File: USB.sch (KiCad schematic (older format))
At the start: 6 parts, among them IC1 TPD2E1B06, J5 USB_OTG

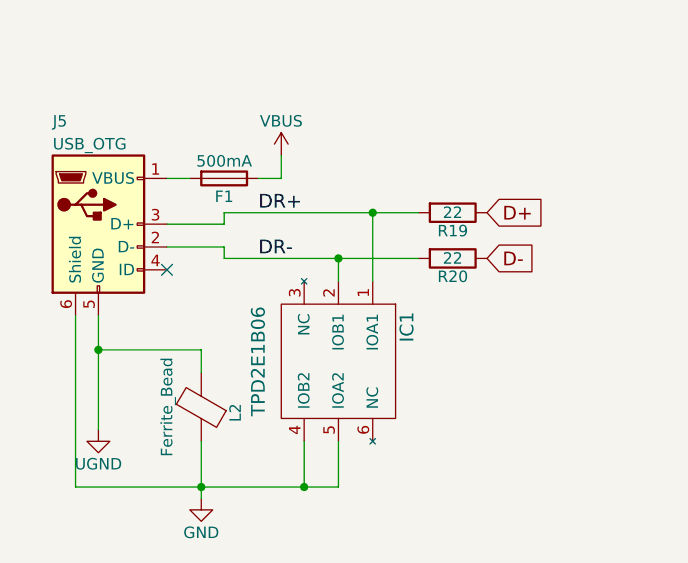
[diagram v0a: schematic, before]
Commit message: Board should be ok. Bargraph leds yet to do.
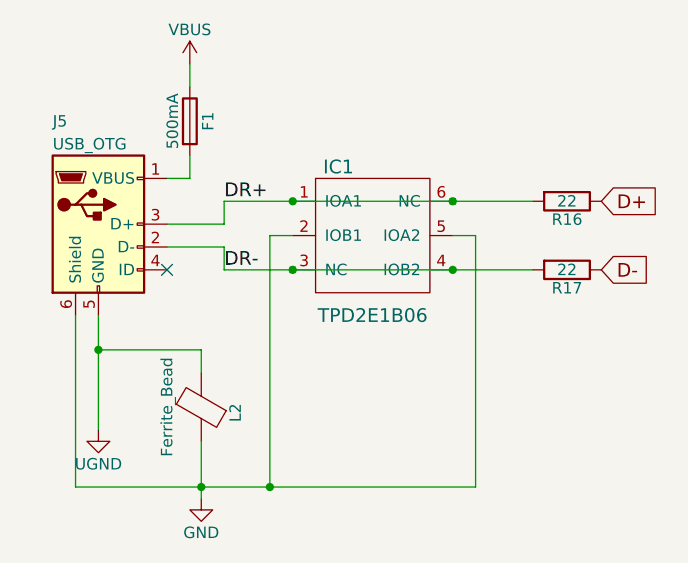
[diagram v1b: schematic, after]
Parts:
- renumbered R19 to R16, R20 to R17
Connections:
- net DR+: now also IC1.6 (NC)
- net DR-: now also IC1.3 (NC), IC1.4 (IOB2); no longer IC1.2 (IOB1)
- net GND: now also IC1.2 (IOB1); no longer IC1.4 (IOB2)
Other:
- moved on the sheet: F1, IC1, R16, R17
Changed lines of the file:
@@
 	1700 4150 1700 4650
 $Comp
-L R R19
+L R R16
 U 1 1 59A9734A
-P 3250 3700
-F 0 "R19" V 3330 3700 50  0000 C CNN
-F 1 "22" V 3250 3700 50  0000 C CNN
-F 2 "Resistors_SMD:R_0603" V 3180 3700 50  0001 C CNN
-F 3 "" H 3250 3700 50  0001 C CNN
-	1    3250 3700
+P 3750 3650
+F 0 "R16" V 3830 3650 50  0000 C CNN
+F 1 "22" V 3750 3650 50  0000 C CNN
+F 2 "Resistors_SMD:R_0603" V 3680 3650 50  0001 C CNN
+F 3 "" H 3750 3650 50  0001 C CNN
+	1    3750 3650
 	0    1    1    0
 $EndComp
 $Comp
-L R R20
+L R R17
 U 1 1 59A973A2
-P 3250 3900
-F 0 "R20" V 3330 3900 50  0000 C CNN
-F 1 "22" V 3250 3900 50  0000 C CNN
-F 2 "Resistors_SMD:R_0603" V 3180 3900 50  0001 C CNN
-F 3 "" H 3250 3900 50  0001 C CNN
-	1    3250 3900
+P 3750 3950
+F 0 "R17" V 3830 3950 50  0000 C CNN
+F 1 "22" V 3750 3950 50  0000 C CNN
+F 2 "Resistors_SMD:R_0603" V 3680 3950 50  0001 C CNN
+F 3 "" H 3750 3950 50  0001 C CNN
+	1    3750 3950
 	0    1    1    0
 $EndComp
@@
 	2000 3850 2250 3850
 Wire Wire Line
-	2250 3850 2250 3900
-Wire Wire Line
-	2250 3900 3100 3900
-Wire Wire Line
 	2000 3750 2250 3750
-Wire Wire Line
-	2250 3750 2250 3700
-Wire Wire Line
-	2250 3700 3100 3700
-Text GLabel 3400 3700 2    60   Input ~ 0
+Text GLabel 3900 3650 2    60   Input ~ 0
 D+
-Text GLabel 3400 3900 2    60   Input ~ 0
+Text GLabel 3900 3950 2    60   Input ~ 0
 D-
 NoConn ~ 2000 3950
-Wire Wire Line
-	2900 4000 2900 3700
-Connection ~ 2900 3700
 $Comp
 L GND #PWR036
@@
 $EndComp
 Wire Wire Line
-	2750 4900 2750 4700
-Wire Wire Line
-	1600 4900 2750 4900
+	1600 4900 3350 4900
 Wire Wire Line
 	2150 4700 2150 4950
@@
 L VBUS #PWR037
 U 1 1 59A98508
-P 2500 3450
-F 0 "#PWR037" H 2500 3300 50  0001 C CNN
-F 1 "VBUS" H 2500 3600 50  0000 C CNN
-F 2 "" H 2500 3450 50  0001 C CNN
-F 3 "" H 2500 3450 50  0001 C CNN
-	1    2500 3450
+P 2100 3050
+F 0 "#PWR037" H 2100 2900 50  0001 C CNN
+F 1 "VBUS" H 2100 3200 50  0000 C CNN
+F 2 "" H 2100 3050 50  0001 C CNN
+F 3 "" H 2100 3050 50  0001 C CNN
+	1    2100 3050
 	1    0    0    -1
 $EndComp
@@
 L Fuse F1
 U 1 1 59B07000
-P 2250 3550
-F 0 "F1" V 2330 3550 50  0000 C CNN
-F 1 "500mA" V 2175 3550 50  0000 C CNN
-F 2 "Fuse_Holders_and_Fuses:Fuse_SMD1206_Reflow" V 2180 3550 50  0001 C CNN
-F 3 "" H 2250 3550 50  0001 C CNN
-	1    2250 3550
-	0    1    1    0
+P 2100 3300
+F 0 "F1" V 2180 3300 50  0000 C CNN
+F 1 "500mA" V 2025 3300 50  0000 C CNN
+F 2 "Fuse_Holders_and_Fuses:Fuse_SMD1206_Reflow" V 2030 3300 50  0001 C CNN
+F 3 "" H 2100 3300 50  0001 C CNN
+	1    2100 3300
+	1    0    0    -1
 $EndComp
 Wire Wire Line
-	2500 3450 2500 3550
-Wire Wire Line
-	2500 3550 2400 3550
+	2100 3050 2100 3150
 Wire Wire Line
 	2000 3550 2100 3550
@@
 	2150 4300 1700 4300
 Connection ~ 1700 4300
+Text Label 2250 3650 0    60   ~ 0
+DR+
+Text Label 2250 3950 0    60   ~ 0
+DR-
+Wire Wire Line
+	2100 3550 2100 3450
 $Comp
 L TPD2E1B06 IC1
 U 1 1 59C9805E
-P 2750 4350
-F 0 "IC1" H 2600 4650 60  0000 C CNN
-F 1 "TPD2E1B06" H 2750 4000 60  0000 C CNN
-F 2 "IC:SOT-5X3" H 2750 4350 60  0001 C CNN
-F 3 "" H 2750 4350 60  0001 C CNN
-	1    2750 4350
-	0    1    1    0
+P 2900 3800
+F 0 "IC1" H 2750 4100 60  0000 C CNN
+F 1 "TPD2E1B06" H 2900 3450 60  0000 C CNN
+F 2 "IC:SOT-5X3" H 2900 3800 60  0001 C CNN
+F 3 "" H 2900 3800 60  0001 C CNN
+	1    2900 3800
+	1    0    0    -1
 $EndComp
 Wire Wire Line
-	2750 4000 2750 3900
-Connection ~ 2750 3900
+	2250 3850 2250 3950
 Wire Wire Line
-	2600 4700 2600 4900
-Connection ~ 2600 4900
-Text Label 2400 3700 0    60   ~ 0
-DR+
-Text Label 2400 3900 0    60   ~ 0
-DR-
+	2250 3950 3600 3950
+Wire Wire Line
+	2250 3750 2250 3650
+Wire Wire Line
+	2250 3650 3600 3650
+Connection ~ 3250 3650
+Connection ~ 2550 3650
+Wire Wire Line
+	3350 4900 3350 3800
+Wire Wire Line
+	3350 3800 3250 3800
+Wire Wire Line
+	2550 3800 2450 3800
+Wire Wire Line
+	2450 3800 2450 4900
+Connection ~ 2450 4900
+Connection ~ 3250 3950
+Connection ~ 2550 3950
 $EndSCHEMATC

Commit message: Board modified after ckecking. Ready for fab, just need to create gerber, position and components files.
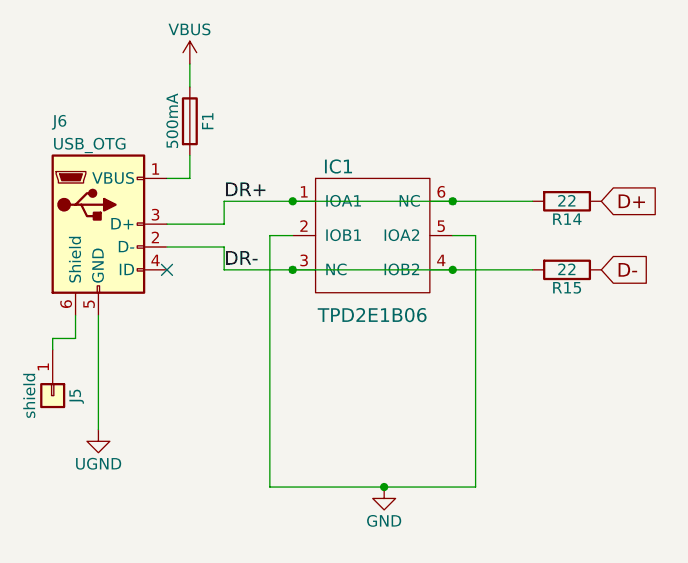
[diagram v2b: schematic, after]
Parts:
- removed L2: Ferrite_Bead, Inductors_SMD:L_0603, symbol Ferrite_Bead
- added J5: shield, Pin_Headers:Pin_Header_Straight_1x01_Pitch2.54mm, symbol Conn_01x01
- renumbered J5 to J6, R16 to R14, R17 to R15
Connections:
- net GND: no longer J6.6 (Shield)
- new net: J5.1 (Pin_1), J6.6 (Shield)
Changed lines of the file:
@@
 EESchema Schematic File Version 2
+LIBS:ContactConsequencesMono-rescue
 LIBS:switches-perso
 LIBS:Logos
@@
 $EndDescr
 $Comp
-L USB_OTG J5
+L USB_OTG J6
 U 1 1 59A96D83
 P 1700 3750
-F 0 "J5" H 1500 4200 50  0000 L CNN
+F 0 "J6" H 1500 4200 50  0000 L CNN
 F 1 "USB_OTG" H 1500 4100 50  0000 L CNN
 F 2 "Connectors:USB_Micro-B" H 1850 3700 50  0001 C CNN
@@
 $EndComp
 $Comp
-L UGND #PWR035
+L UGND #PWR037
 U 1 1 59A9730E
 P 1700 4650
-F 0 "#PWR035" H 1700 4400 50  0001 C CNN
+F 0 "#PWR037" H 1700 4400 50  0001 C CNN
 F 1 "UGND" H 1700 4500 50  0000 C CNN
 F 2 "" H 1700 4650 50  0001 C CNN
@@
 	1    0    0    -1
 $EndComp
-Wire Wire Line
-	1700 4150 1700 4650
-$Comp
-L R R16
+$Comp
+L R R14
 U 1 1 59A9734A
 P 3750 3650
-F 0 "R16" V 3830 3650 50  0000 C CNN
+F 0 "R14" V 3830 3650 50  0000 C CNN
 F 1 "22" V 3750 3650 50  0000 C CNN
 F 2 "Resistors_SMD:R_0603" V 3680 3650 50  0001 C CNN
@@
 $EndComp
 $Comp
-L R R17
+L R R15
 U 1 1 59A973A2
 P 3750 3950
-F 0 "R17" V 3830 3950 50  0000 C CNN
+F 0 "R15" V 3830 3950 50  0000 C CNN
 F 1 "22" V 3750 3950 50  0000 C CNN
 F 2 "Resistors_SMD:R_0603" V 3680 3950 50  0001 C CNN
@@
 	0    1    1    0
 $EndComp
-Wire Wire Line
-	2000 3850 2250 3850
-Wire Wire Line
-	2000 3750 2250 3750
 Text GLabel 3900 3650 2    60   Input ~ 0
 D+
@@
 NoConn ~ 2000 3950
 $Comp
-L GND #PWR036
+L GND #PWR038
 U 1 1 59A98308
-P 2150 4950
-F 0 "#PWR036" H 2150 4700 50  0001 C CNN
-F 1 "GND" H 2150 4800 50  0000 C CNN
-F 2 "" H 2150 4950 50  0001 C CNN
-F 3 "" H 2150 4950 50  0001 C CNN
-	1    2150 4950
-	1    0    0    -1
-$EndComp
-Wire Wire Line
-	1600 4900 3350 4900
-Wire Wire Line
-	2150 4700 2150 4950
-Wire Wire Line
-	1600 4900 1600 4150
-Connection ~ 2150 4900
-$Comp
-L VBUS #PWR037
+P 2950 4900
+F 0 "#PWR038" H 2950 4650 50  0001 C CNN
+F 1 "GND" H 2950 4750 50  0000 C CNN
+F 2 "" H 2950 4900 50  0001 C CNN
+F 3 "" H 2950 4900 50  0001 C CNN
+	1    2950 4900
+	1    0    0    -1
+$EndComp
+$Comp
+L VBUS #PWR039
 U 1 1 59A98508
 P 2100 3050
-F 0 "#PWR037" H 2100 2900 50  0001 C CNN
+F 0 "#PWR039" H 2100 2900 50  0001 C CNN
 F 1 "VBUS" H 2100 3200 50  0000 C CNN
 F 2 "" H 2100 3050 50  0001 C CNN
@@
 	1    0    0    -1
 $EndComp
-Wire Wire Line
-	2100 3050 2100 3150
-Wire Wire Line
-	2000 3550 2100 3550
-$Comp
-L Ferrite_Bead L2
-U 1 1 59B1BF09
-P 2150 4550
-F 0 "L2" V 2000 4575 50  0000 C CNN
-F 1 "Ferrite_Bead" V 2300 4550 50  0000 C CNN
-F 2 "Inductors_SMD:L_0603" V 2080 4550 50  0001 C CNN
-F 3 "" H 2150 4550 50  0001 C CNN
-	1    2150 4550
-	-1   0    0    1
-$EndComp
-Wire Wire Line
-	2150 4400 2150 4300
-Wire Wire Line
-	2150 4300 1700 4300
-Connection ~ 1700 4300
 Text Label 2250 3650 0    60   ~ 0
 DR+
 Text Label 2250 3950 0    60   ~ 0
 DR-
-Wire Wire Line
-	2100 3550 2100 3450
 $Comp
 L TPD2E1B06 IC1
@@
 $EndComp
 Wire Wire Line
+	1700 4150 1700 4650
+Wire Wire Line
+	2000 3850 2250 3850
+Wire Wire Line
+	2000 3750 2250 3750
+Wire Wire Line
+	2100 3050 2100 3150
+Wire Wire Line
+	2000 3550 2100 3550
+Wire Wire Line
+	2100 3550 2100 3450
+Wire Wire Line
 	2250 3850 2250 3950
 Wire Wire Line
@@
 Wire Wire Line
 	2550 3800 2450 3800
-Wire Wire Line
-	2450 3800 2450 4900
-Connection ~ 2450 4900
 Connection ~ 3250 3950
 Connection ~ 2550 3950
+Wire Wire Line
+	2450 3800 2450 4900
+Wire Wire Line
+	2450 4900 3350 4900
+Connection ~ 2950 4900
+$Comp
+L Conn_01x01 J5
+U 1 1 59F09009
+P 1500 4500
+F 0 "J5" H 1500 4600 50  0000 C CNN
+F 1 "shield" H 1500 4400 50  0000 C CNN
+F 2 "Pin_Headers:Pin_Header_Straight_1x01_Pitch2.54mm" H 1500 4500 50  0001 C CNN
+F 3 "" H 1500 4500 50  0001 C CNN
+	1    1500 4500
+	0    1    1    0
+$EndComp
+Wire Wire Line
+	1600 4150 1600 4250
+Wire Wire Line
+	1600 4250 1500 4250
+Wire Wire Line
+	1500 4250 1500 4300
 $EndSCHEMATC
